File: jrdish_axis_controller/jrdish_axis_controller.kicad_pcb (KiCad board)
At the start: 4 copper layers, 100 x 100 mm, 201 parts, among them CN1 KF2EDGR-2.54-9P, CN10 KF2EDGR-2.54-2P, CN11 KF2EDGR-2.54-3P, CN12 KF2EDGR-2.54-9P, CN13 KF2EDGR-2.54-6P, CN14 KF2EDGR-2.54-6P, CN2 KF2EDGR-2.54-6P, CN3 KF2EDGR-2.54-4P, CN4 KF2EDGR-2.54-4P, CN5 KF2EDGR-2.54-4P, CN6 KF2EDGR-2.54-2P, CN7 SM04B-SRSS-TB (LF)(SN), CN8 SM04B-SRSS-TB (LF)(SN), CN9 KF2EDGR-2.54-2P, J1 Conn_ARM_SWD_TagConnect_TC2030, M1 MountingHole_2.7mm_M2.5_ISO14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, Q1 AO3407A, Q2 AO3400A, Q3 2N7002, SW1 DSHP04TSGER, SW2 SS-12F49-G050, U1 STM32G474RET6, U2 ISOW1432BDFMR, U3 ISOW1432BDFMR, U4 MP2322GQH-Z, U5 LTC4311ISC6#TRPBF, U6 LM75BIMX-5/NOPB, U7 W25Q32JVSSIQ_C179173, U8 SP3232EEY-L/TR, X1 NX2016SA-16MHZ-EXS00A-CS07826

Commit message: Making refinements
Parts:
- added D18: TPESD0402G05V, MyParts:D0402-BI, F.Cu at (153.8, 121.0)
- added D19: TPESD0402G05V, MyParts:D0402-BI, F.Cu at (158.8, 121.0)
- added D20: TPESD0402G05V, MyParts:D0402-BI, F.Cu at (163.8, 121.0)
- added D21: TPESD0402G05V, MyParts:D0402-BI, F.Cu at (194.0, 121.0)
- added D22: TPESD0402G05V, MyParts:D0402-BI, F.Cu at (199.2, 121.0)
- added D23: TPESD0402G05V, MyParts:D0402-BI, F.Cu at (204.1, 121.1)
- added D24: TPESD0402G05V, MyParts:D0402-BI, F.Cu at (201.2, 83.6)
- added R57: 100Ω, PCM_JLCPCB:R_0402, F.Cu at (153.8, 118.8)
- added R58: 100Ω, PCM_JLCPCB:R_0402, F.Cu at (158.8, 118.7)
- added R59: 100Ω, PCM_JLCPCB:R_0402, F.Cu at (163.8, 118.7)
- added R60: 100Ω, PCM_JLCPCB:R_0402, F.Cu at (194.0, 118.7)
- added R61: 100Ω, PCM_JLCPCB:R_0402, F.Cu at (199.2, 118.7)
- added R62: 100Ω, PCM_JLCPCB:R_0402, F.Cu at (204.1, 118.8)
- added R63: 10kΩ, PCM_JLCPCB:R_0402, F.Cu at (201.2, 79.3)
- added R64: 10kΩ, PCM_JLCPCB:R_0402, F.Cu at (185.3, 99.5)
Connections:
- CN13 pad 2: PUL2_MCU -> Net-(D21-K)
- CN13 pad 4: DIR2_MCU -> Net-(D22-K)
- CN13 pad 6: ENABLE2_MCU -> Net-(D23-K)
- CN2 pad 2: PUL1_MCU -> Net-(D18-K)
- CN2 pad 4: DIR1_MCU -> Net-(D19-K)
- CN2 pad 6: ENABLE1_MCU -> Net-(D20-K)
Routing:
- net ENABLE1_MCU: track 33.5 -> 26.0 mm
- net Net-(D19-K): track 0.00 -> 6.11 mm
- net Net-(D22-K): track 0.00 -> 6.01 mm
- net Net-(D21-K): track 0.00 -> 5.98 mm
- net Net-(D23-K): track 0.00 -> 5.85 mm
- net PUL1_MCU: track 28.8 -> 23.0 mm
- net PUL2_MCU: track 55.6 -> 49.8 mm
- net Net-(D18-K): track 0.00 -> 5.69 mm
- net Net-(D20-K): track 0.00 -> 5.66 mm
- net DIR1_MCU: track 29.3 -> 24.1 mm
- net DIR2_MCU: track 58.8 -> 54.4 mm
- net ENABLE2_MCU: track 66.8 -> 62.6 mm
- net FLASH_CS_MCU: track 25.6 -> 27.3 mm
- net Net-(D24-K): track 5.20 -> 6.59 mm
- net 3V3: track 85.0 -> 86.3 mm, vias 58 -> 59
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
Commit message: Making refinements
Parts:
- added TP1: RH-5016, MyParts:TESTPOINT-SMD_L3.0-W2.0, F.Cu at (137.4, 93.8)
- added TP2: RH-5016, MyParts:TESTPOINT-SMD_L3.0-W2.0, F.Cu at (119.3, 113.8)
- added TP3: RH-5016, MyParts:TESTPOINT-SMD_L3.0-W2.0, F.Cu at (136.8, 100.1)
- added TP4: RH-5016, MyParts:TESTPOINT-SMD_L3.0-W2.0, F.Cu at (199.4, 64.5)
- C49: value 100nF -> 10uF; footprint PCM_JLCPCB:C_0603 -> PCM_JLCPCB:C_0805
- C50: footprint PCM_JLCPCB:C_0603 -> PCM_JLCPCB:C_0805
- C51: value 10uF -> 100nF
- moved R22 7.38 mm to (128.7, 106.4), turned to 0 degrees
- moved C52 3.78 mm to (129.1, 109.7)
- moved R21 1.47 mm to (129.0, 108.0)
- moved R23 1.39 mm to (125.9, 108.0)
- moved C53 1.35 mm to (124.6, 102.8)
- moved C54 1.35 mm to (123.4, 107.7)
- moved U4 1.35 mm to (123.7, 105.7)
- moved C48 1.35 mm to (125.3, 104.9)
- moved L11 1.35 mm to (128.4, 103.6)
- moved C51 1.25 mm to (121.7, 105.6)
- moved C50 0.98 mm to (119.9, 105.5)
- moved C49 0.56 mm to (117.9, 105.5)
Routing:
- net 3V3: track 86.3 -> 99.3 mm, vias 59 -> 60
- net Net-(U4-VCC): track 2.70 -> 11.9 mm, vias 0 -> 2
- net /Power/12V_IN: track 9.98 -> 17.9 mm
- net 12V: track 62.5 -> 65.6 mm, vias 7 -> 15
- net Net-(U4-PG): track 6.15 -> 3.76 mm, vias 2 -> 0
- net GND: track 26.3 -> 27.6 mm, vias 262 -> 285
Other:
- board text added: "12V IN"
- board text added: "3.3V"
- board text added: "Axis Commander V1.0 JRSeti www.jrseti.com"
- board text added: "FAN 12V"
- board text added: "RS232/3.3V Jumpers"
- board text removed: "FAN"

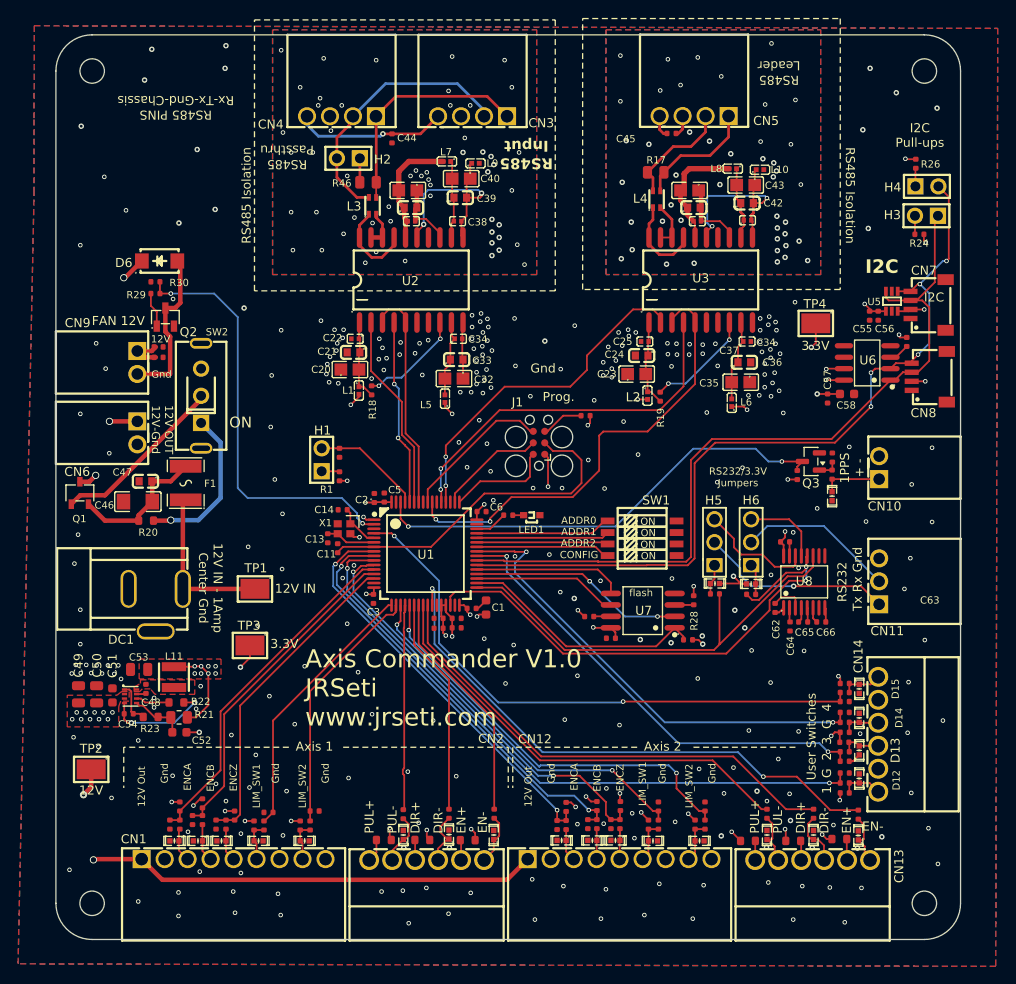
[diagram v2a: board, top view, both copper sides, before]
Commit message: Limit switches with mosfets
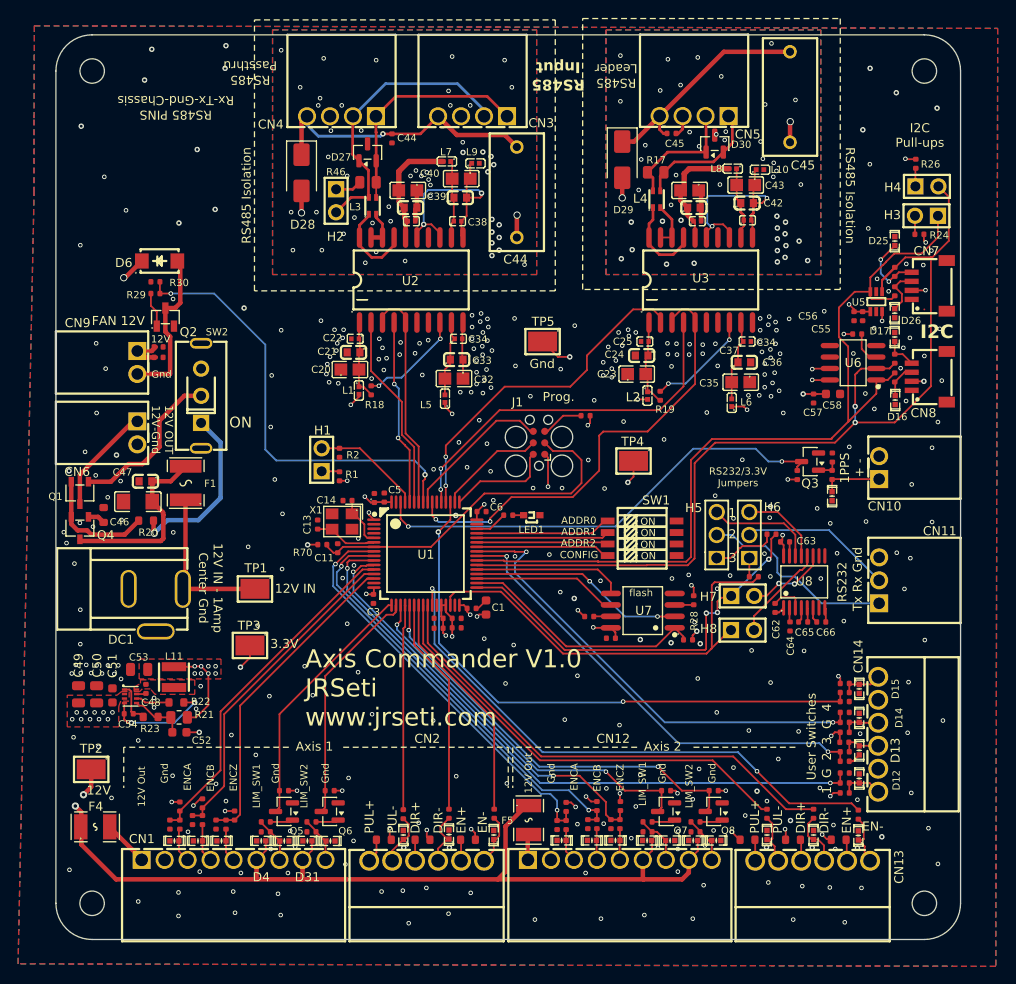
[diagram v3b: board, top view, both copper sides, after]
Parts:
- removed C18, C19, C70, C71: 100nF, PCM_JLCPCB:C_0402
- removed R10, R11, R39, R40: 10kΩ, PCM_JLCPCB:R_0402
- removed R12, R13, R41, R42: 100Ω, PCM_JLCPCB:R_0402
- added C44: 10nF, MyParts:CAP-TH_L13.0-W6.0-P10.00-D1.2, F.Cu at (166.3, 50.0)
- added C45: 10nF, MyParts:CAP-TH_L13.0-W6.0-P10.00-D1.2, F.Cu at (196.6, 39.5)
- added D25: TPESD0402G05V, MyParts:D0402-BI, F.Cu at (208.1, 55.4)
- added D26: TPESD0402G05V, MyParts:D0402-BI, F.Cu at (208.1, 63.4)
- added D27: SM712_SOT23, Package_TO_SOT_SMD:SOT-23, F.Cu at (149.8, 45.6)
- added D28: SMAJ15CA, Diode_SMD:D_SMA, F.Cu at (142.6, 47.9)
- added D29: SMAJ15CA, Diode_SMD:D_SMA, F.Cu at (178.0, 46.4)
- added D30: SM712_SOT23, Package_TO_SOT_SMD:SOT-23, F.Cu at (188.2, 44.6)
- added D31: TPESD0402G05V, MyParts:D0402-BI, F.Cu at (143.2, 121.7)
- added D32: TPESD0402G05V, MyParts:D0402-BI, F.Cu at (145.8, 121.7)
- added D33: TPESD0402G05V, MyParts:D0402-BI, F.Cu at (185.8, 121.7)
- added D34: TPESD0402G05V, MyParts:D0402-BI, F.Cu at (188.4, 121.7)
- added F4: MF-USMF020-2, MyParts:F1210, F.Cu at (119.8, 120.2)
- added F5: MF-USMF020-2, MyParts:F1210, F.Cu at (167.7, 119.4)
- added H7: 210S-1*2P L=11.6MMGold-plated black, MyParts:HDR-TH_2P-P2.54-V-M-1, F.Cu at (191.3, 94.6)
- added H8: 210S-1*2P L=11.6MMGold-plated black, MyParts:HDR-TH_2P-P2.54-V-M-1, F.Cu at (191.3, 98.4)
- added Q4: AO3407A, MyParts:SOT-23-3_L2.9-W1.6-P1.90-LS2.8-BR, F.Cu at (118.0, 87.1)
- added Q5: BSS138, Package_TO_SOT_SMD:SOT-23, F.Cu at (140.6, 118.5)
- added Q6: BSS138, Package_TO_SOT_SMD:SOT-23, F.Cu at (145.7, 118.5)
- added Q7: BSS138, Package_TO_SOT_SMD:SOT-23, F.Cu at (182.8, 118.5)
- added Q8: BSS138, Package_TO_SOT_SMD:SOT-23, F.Cu at (188.1, 118.5)
- added R65: 10kΩ, PCM_JLCPCB:R_0603, F.Cu at (120.7, 85.7)
- added R66: 22Ω, PCM_JLCPCB:R_0402, F.Cu at (208.1, 58.8)
- added R67: 22Ω, PCM_JLCPCB:R_0402, F.Cu at (208.1, 61.0)
- added R68: 22Ω, PCM_JLCPCB:R_0402, F.Cu at (208.1, 68.4)
- added R69: 22Ω, PCM_JLCPCB:R_0402, F.Cu at (208.1, 70.5)
- added R70: 10kΩ, PCM_JLCPCB:R_0402, F.Cu at (144.8, 89.0)
- added R71: 100kΩ, PCM_JLCPCB:R_0402, F.Cu at (138.6, 120.7)
- added R72: 10kΩ, PCM_JLCPCB:R_0402, F.Cu at (138.6, 119.6)
- added R73: 10kΩ, PCM_JLCPCB:R_0402, F.Cu at (140.6, 116.2)
- added R74: 100kΩ, PCM_JLCPCB:R_0402, F.Cu at (143.7, 120.7)
- added R75: 10kΩ, PCM_JLCPCB:R_0402, F.Cu at (143.7, 119.6)
- added R76: 10kΩ, PCM_JLCPCB:R_0402, F.Cu at (145.7, 116.2)
- added R77: 100kΩ, PCM_JLCPCB:R_0402, F.Cu at (180.8, 120.7)
- added R78: 10kΩ, PCM_JLCPCB:R_0402, F.Cu at (180.8, 119.6)
- added R79: 10kΩ, PCM_JLCPCB:R_0402, F.Cu at (182.8, 116.2)
- added R80: 100kΩ, PCM_JLCPCB:R_0402, F.Cu at (186.1, 120.7)
- added R81: 10kΩ, PCM_JLCPCB:R_0402, F.Cu at (186.1, 119.6)
- added R82: 10kΩ, PCM_JLCPCB:R_0402, F.Cu at (188.1, 116.2)
- added TP5: RH-5016, MyParts:TESTPOINT-SMD_L3.0-W2.0, F.Cu at (169.2, 66.5)
- C13, C14: value 6.8pF -> 33pF
- Q3: value 2N7002 -> BSS138
- R14, R15, R16, R43, R44, R45: value 270Ω -> 180Ω
- R18, R19: value 4.7kΩ -> 5.1kΩ
- R32: value 10kΩ -> 100Ω
- U6: value LM75BIMX-5/NOPB -> LM75BIMX-3/NOPB
- X1: value NX2016SA-16MHZ-EXS00A-CS07826 -> 7M-16.000MAAJ-T; footprint MyParts:CRYSTAL-SMD_4P-L2.0-W1.6-BL -> MyParts:OSC-SMD_4P-L3.2-W2.5-BL-OXETDLJANF-0.032768MHZ
- moved D17 31.6 mm to (208.1, 66.0), turned to 90 degrees
- moved D16 28.4 mm to (208.2, 73.0), turned to -90 degrees
- moved TP4 25.2 mm to (179.2, 79.7)
- moved R55 9.09 mm to (194.5, 87.8), turned to 0 degrees
- moved R25 5.54 mm to (204.0, 65.7), turned to 180 degrees
- moved H2 4.89 mm to (146.4, 50.9), turned to -90 degrees
- moved D11 3.25 mm to (183.3, 121.7)
- moved D5 2.25 mm to (140.7, 121.7)
- moved CN7 2.11 mm to (211.9, 60.4)
- moved R56 1.97 mm to (192.6, 92.5), turned to 0 degrees
- moved C13 1.88 mm to (144.3, 86.7), turned to 90 degrees
- moved U5 1.73 mm to (206.1, 62.1)
- moved C56 1.73 mm to (204.6, 63.7)
- moved C55 1.73 mm to (203.6, 63.7)
- moved U6 1.56 mm to (203.5, 68.8)
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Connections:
- net ENC1_A renamed /Axis Control - 1/ENC1_A
- net ENC1_B renamed /Axis Control - 1/ENC1_B
- net ENC1_Z renamed /Axis Control - 1/ENC1_Z
- net ENC2_A renamed /Axis Control - 2/ENC2_A
- net ENC2_B renamed /Axis Control - 2/ENC2_B
- net ENC2_Z renamed /Axis Control - 2/ENC2_Z
- CN1 pad 1: 12V -> Net-(CN1-Pad1)
- CN1 pad 6: /Axis Control - 1/LIM1_SW1_OUT -> 12V
- CN1 pad 7: GND -> /Axis Control - 1/LIM1_SW1_RETURN
- CN1 pad 8: /Axis Control - 1/LIM1_SW2_OUT -> 12V
- CN1 pad 9: GND -> /Axis Control - 1/LIM1_SW2_RETURN
- CN12 pad 1: 12V -> Net-(CN12-Pad1)
- CN12 pad 6: /Axis Control - 2/LIM2_SW1_OUT -> 12V
- CN12 pad 7: GND -> /Axis Control - 2/LIM2_SW1_RETURN
- CN12 pad 8: /Axis Control - 2/LIM2_SW2_OUT -> 12V
- CN12 pad 9: GND -> /Axis Control - 2/LIM2_SW2_RETURN
- CN7 pad 3: SDA_MCU -> Net-(D26-K)
- CN7 pad 4: SCL_MCU -> Net-(D25-K)
- CN8 pad 3: SDA_MCU -> Net-(D16-K)
- CN8 pad 4: SCL_MCU -> Net-(D17-K)
- D10 pad 1: /Axis Control - 2/LIM2_SW1_OUT -> 12V
- D11 pad 1: /Axis Control - 2/LIM2_SW2_OUT -> /Axis Control - 2/LIM2_SW1_RETURN
- D4 pad 1: /Axis Control - 1/LIM1_SW1_OUT -> 12V
- D5 pad 1: /Axis Control - 1/LIM1_SW2_OUT -> /Axis Control - 1/LIM1_SW1_RETURN
- H5 pad 1: Net-(D16-K) -> Net-(H5-Pad1)
- H6 pad 1: Net-(D17-K) -> Net-(H6-Pad1)
- Q1 pad 2: /Power/12V_IN_FUSED -> Net-(Q1-S)
- R20 pad 1: /Power/12V_IN_FUSED -> Net-(Q1-S)
- R55 pad 1: RS232_TX_MCU -> Net-(H5-Pad1)
- R55 pad 2: Net-(D16-K) -> RS232_TX_MCU
- R56 pad 1: Net-(D17-K) -> Net-(H6-Pad1)
- U1 pad 2: FAN_MCU -> unconnected-(U1-PC13-Pad2)
- U1 pad 4: USER_SW_4_MCU -> unconnected-(U1-PC15-OSC32_OUT-Pad4)
- U1 pad 51: unconnected-(U1-PA15-Pad51) -> USER_SW_4_MCU
- U1 pad 57: unconnected-(U1-PB4-Pad57) -> FAN_MCU
- U2 pad 13: RS485_1_GND -> Net-(U2-GISOIN)
- U3 pad 13: RS485_2_GND -> Net-(U3-GISOIN)
- U8 pad 11: RS232_TX_MCU -> /GPS RS232/T1IN
- U8 pad 12: RS232_RX_MCU -> /GPS RS232/R1OUT
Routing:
- net 12V: track 65.6 -> 124.1 mm, vias 15 -> 13
- net /RS485/RS485_2_CHASSIS: track 2.50 -> 25.2 mm
- net SCL_MCU: track 91.4 -> 109.4 mm, vias 5 -> 2
- net /RS485/RS485_1_CHASSIS: track 16.9 -> 31.5 mm
- net Net-(Q1-S): track 0.00 -> 13.3 mm
- net /GPS RS232/R1OUT: track 0.00 -> 10.8 mm
- net RS232_RX_MCU: track 58.7 -> 48.7 mm, vias 2 -> 0
- net /GPS RS232/T1IN: track 0.00 -> 9.01 mm, vias 0 -> 2
- net SDA_MCU: track 89.0 -> 97.1 mm
- net Net-(D25-K): track 0.00 -> 7.94 mm, vias 0 -> 2
- net Net-(H5-Pad1): track 0.00 -> 7.25 mm
- net /Axis Control - 2/LIM2_SW1_RETURN: track 0.00 -> 5.56 mm
- net /Axis Control - 2/LIM2_SW2_RETURN: track 0.00 -> 5.35 mm
- net Net-(D26-K): track 0.00 -> 5.20 mm
- net RS232_TX_MCU: track 50.6 -> 45.5 mm, vias 0 -> 3
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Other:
- board text added: "1"
- board text added: "2"
- board text added: "3"
